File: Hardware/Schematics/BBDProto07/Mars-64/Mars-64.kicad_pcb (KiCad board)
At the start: 4 copper layers, 45.7 x 101.6 mm, 79 parts, among them U101 ADG731, U102 ADG731

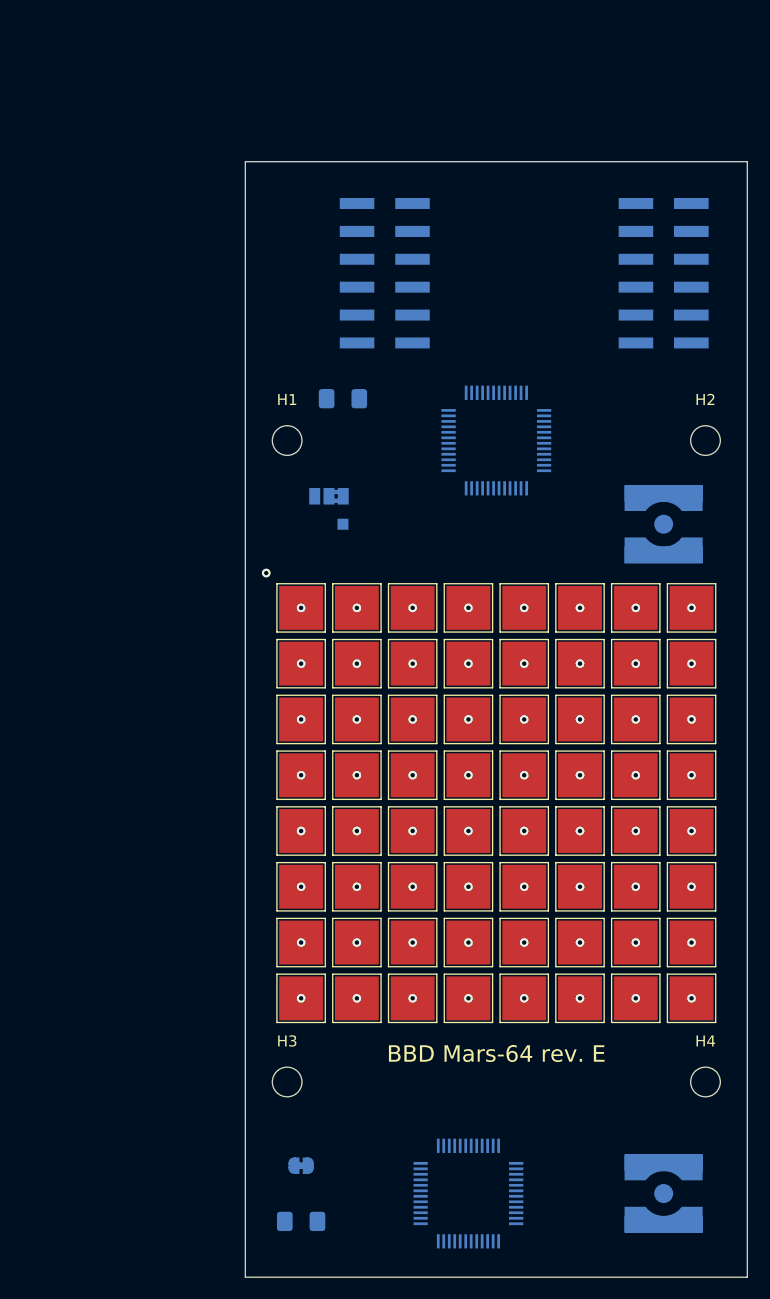
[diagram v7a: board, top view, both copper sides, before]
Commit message: Finished the routing for Mars-64 rev. E
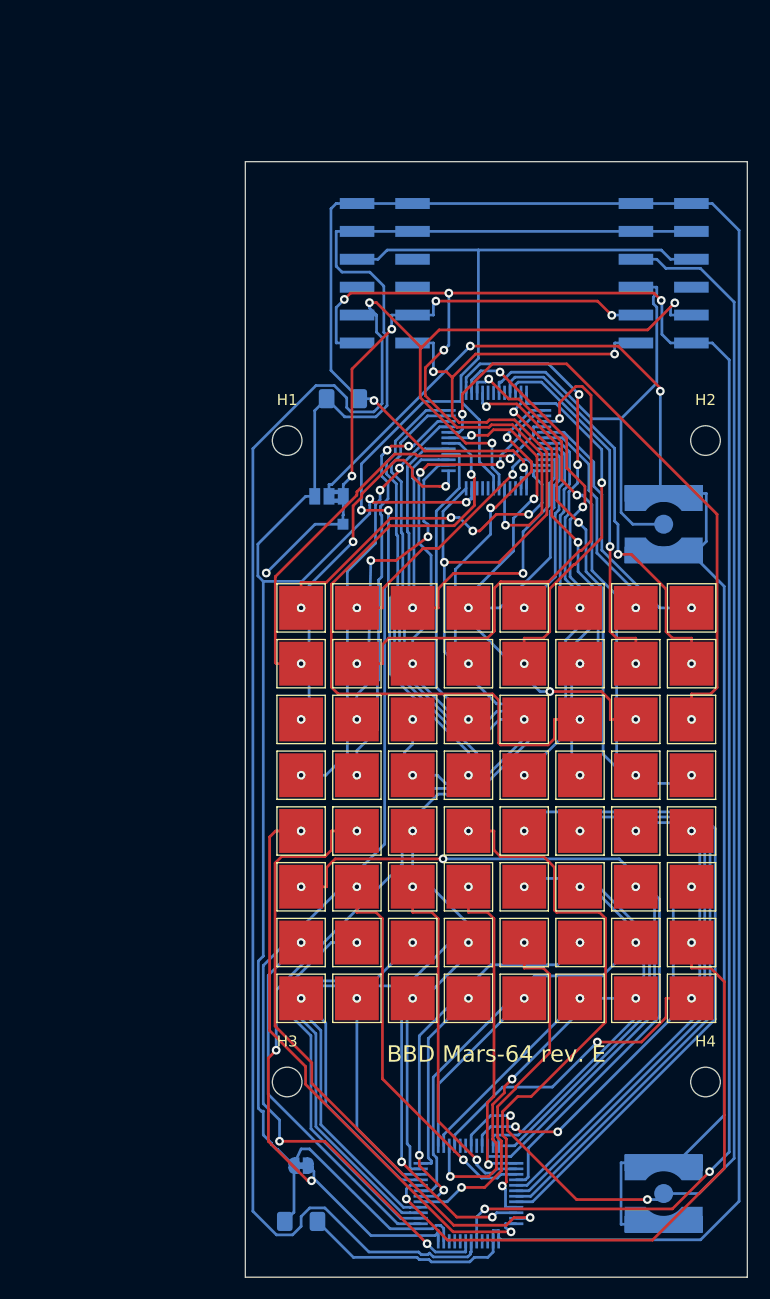
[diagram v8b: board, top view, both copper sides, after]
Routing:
- net /VCC3V3: track 0.00 -> 211.4 mm, vias 0 -> 2
- net GND: track 0.00 -> 181.6 mm, vias 0 -> 2
- net /~SPI_CE: track 0.00 -> 181.4 mm, vias 0 -> 7
- net /SPI_MOSI: track 0.00 -> 174.0 mm, vias 0 -> 3
- net /SPI_CLK: track 0.00 -> 157.8 mm, vias 0 -> 4
- net /VSS: track 0.00 -> 155.1 mm, vias 0 -> 5
- net Net-(J101-Pad2): track 0.00 -> 133.3 mm, vias 0 -> 2
- net /DB: track 0.00 -> 120.1 mm, vias 0 -> 2
- net Net-(TP209-Pad1): track 0.00 -> 67.7 mm, vias 1 -> 2
- net Net-(TP122-Pad1): track 0.00 -> 61.7 mm, vias 1 -> 2
- net Net-(TP205-Pad1): track 0.00 -> 61.1 mm
- net Net-(TP224-Pad1): track 0.00 -> 58.4 mm, vias 1 -> 2
- net Net-(TP119-Pad1): track 0.00 -> 58.1 mm
- net Net-(TP202-Pad1): track 0.00 -> 58.0 mm, vias 1 -> 2
- net Net-(TP124-Pad1): track 0.00 -> 55.3 mm, vias 1 -> 2
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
